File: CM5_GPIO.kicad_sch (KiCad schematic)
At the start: 29 parts, among them J14 JST_SHBM04B-SRSS-TB, J16 JST_SHBM04B-SRSS-TB, J2 Conn_02x07_Odd_Even, J3 Conn_01x03, J7 Micro_SD_Card_Det, J8 THD-20-R, J9 THD-02-R, SW1 Right angle Tact button, SW2 Right angle Tact button, U1 TPD4EUSB30, U18 RT9742GGJ5, U2 TPD4EUSB30, U3 MagJack-A70-112-331N126, U5 74LVC1G07SE-7, U9 SK6812

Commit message: starting to trace
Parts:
- added J19: Conn_01x03, Connector_PinHeader_2.54mm:PinHeader_1x03_P2.54mm_Vertical, symbol Connector_Generic:Conn_01x03
- SW2: footprint Button_Switch_THT:SW_Tactile_SPST_Angled_PTS645Vx58-2LFS -> Button_Switch_THT:SW_Tactile_SPST_Angled_PTS645Vx31-2LFS
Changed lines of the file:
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@@
 			)
 		)
-		(property "Footprint" "Button_Switch_THT:SW_Tactile_SPST_Angled_PTS645Vx58-2LFS"
+		(property "Footprint" "Button_Switch_THT:SW_Tactile_SPST_Angled_PTS645Vx31-2LFS"
 			(at 86.36 158.75 0)
 			(effects
@@
 					(unit 1)
 				)
+			)
+		)
+	)
+	(symbol
+		(lib_id "Connector_Generic:Conn_01x03")
+		(at 143.51 113.03 0)
+		(unit 1)
+		(exclude_from_sim no)
+		(in_bom yes)
+		(on_board yes)
+		(dnp no)
+		(fields_autoplaced yes)
+		(property "Reference" "J19"
+			(at 146.05 111.7599 0)
+			(effects
+				(font
+					(size 1.27 1.27)
+				)
+				(justify left)
+			)
+		)
+		(property "Value" "Conn_01x03"
+			(at 146.05 114.2999 0)
+			(effects
+				(font
+					(size 1.27 1.27)
+				)
+				(justify left)
+			)
+		)
+		(property "Footprint" "Connector_PinHeader_2.54mm:PinHeader_1x03_P2.54mm_Vertical"
+			(at 143.51 113.03 0)
+			(effects
+				(font
+					(size 1.27 1.27)
+				)
+				(hide yes)
+			)
+		)
+		(property "Datasheet" "~"
+			(at 143.51 113.03 0)
+			(effects
+				(font
+					(size 1.27 1.27)
+				)
+				(hide yes)
+			)
+		)
+		(property "Description" "Generic connector, single row, 01x03, script generated (kicad-library-utils/schlib/autogen/connector/)"
+			(at 143.51 113.03 0)
+			(effects
+				(font
+					(size 1.27 1.27)
+				)
+				(hide yes)
+			)
+		)
+		(pin "2"
+		)
+		(pin "3"
+		)
+		(pin "1"
+		)
+		(instances
+			(project ""
+				(path "/e63e39d7-6ac0-4ffd-8aa3-1841a4541b55/00000000-0000-0000-0000-00005cff706a"
+					(reference "J19")
+					(unit 1)
+				)

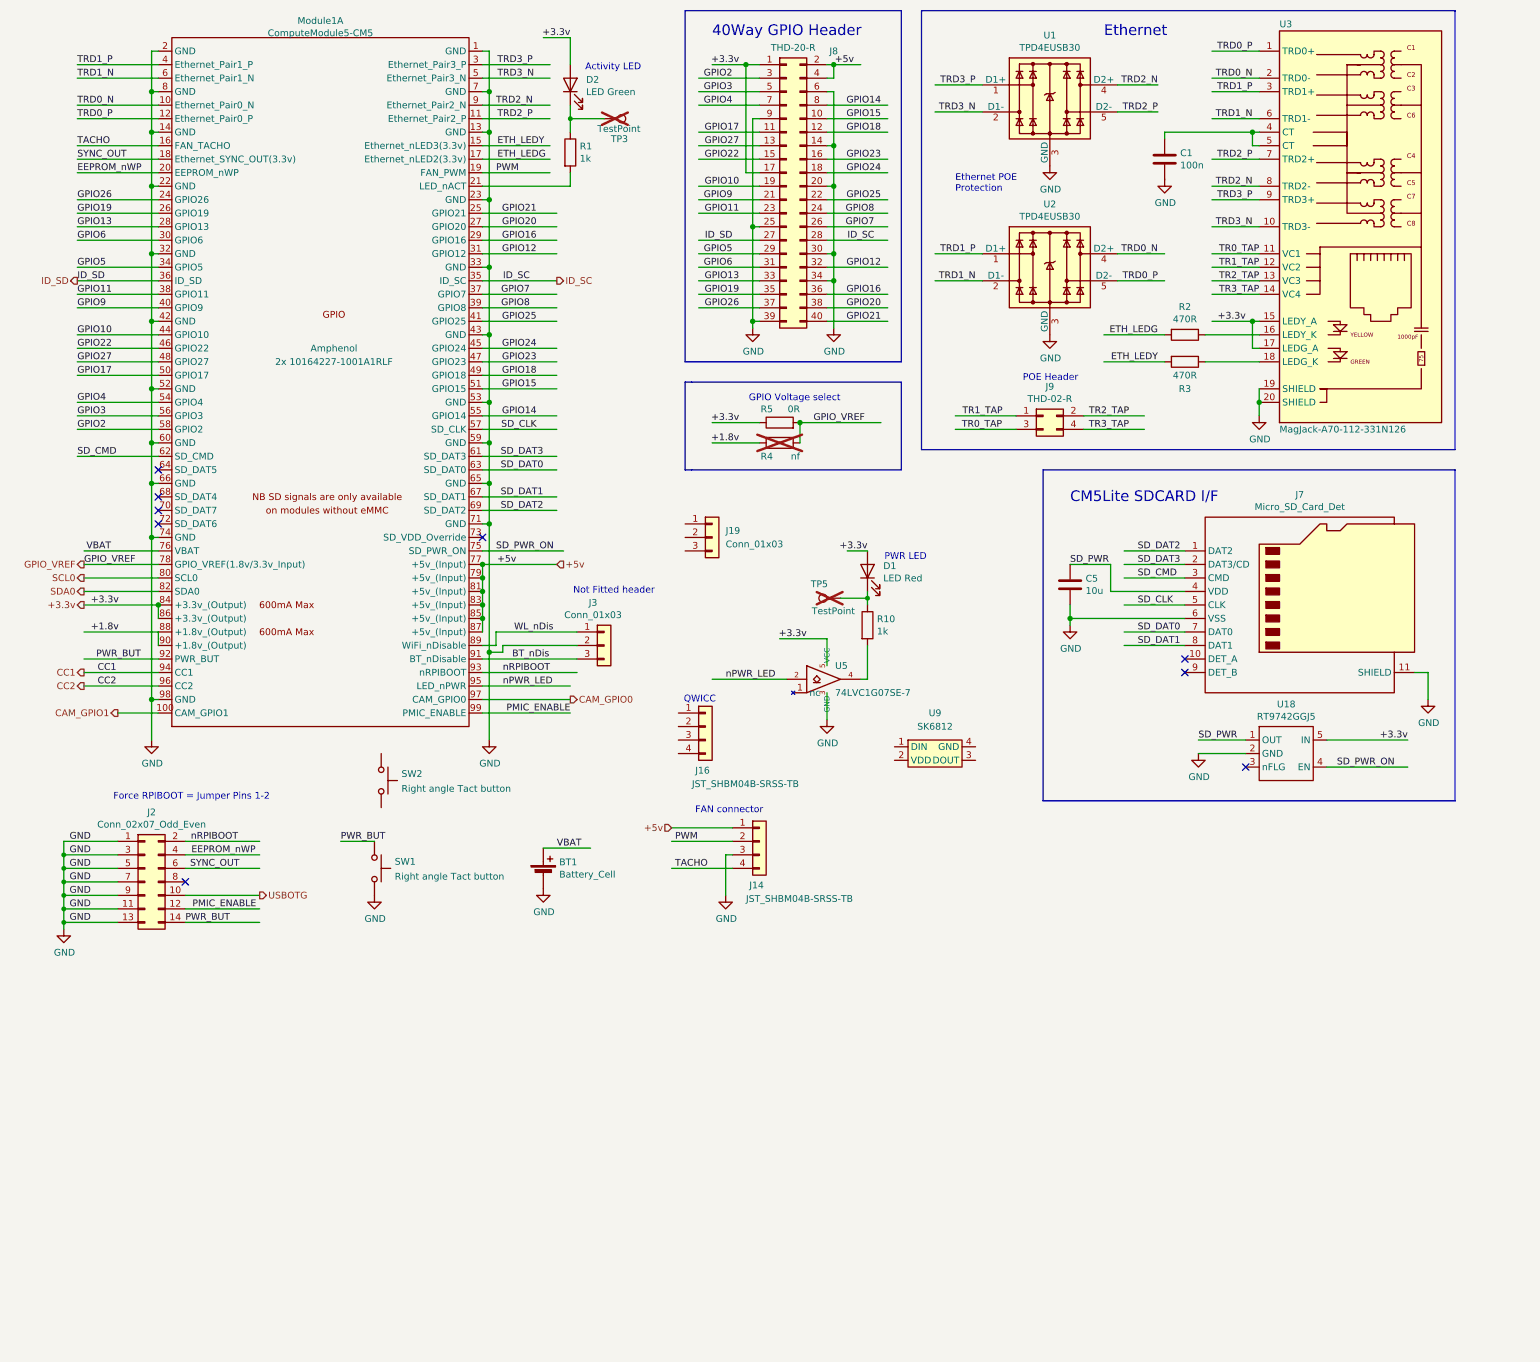
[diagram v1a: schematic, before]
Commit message: voltage regulator refactoring
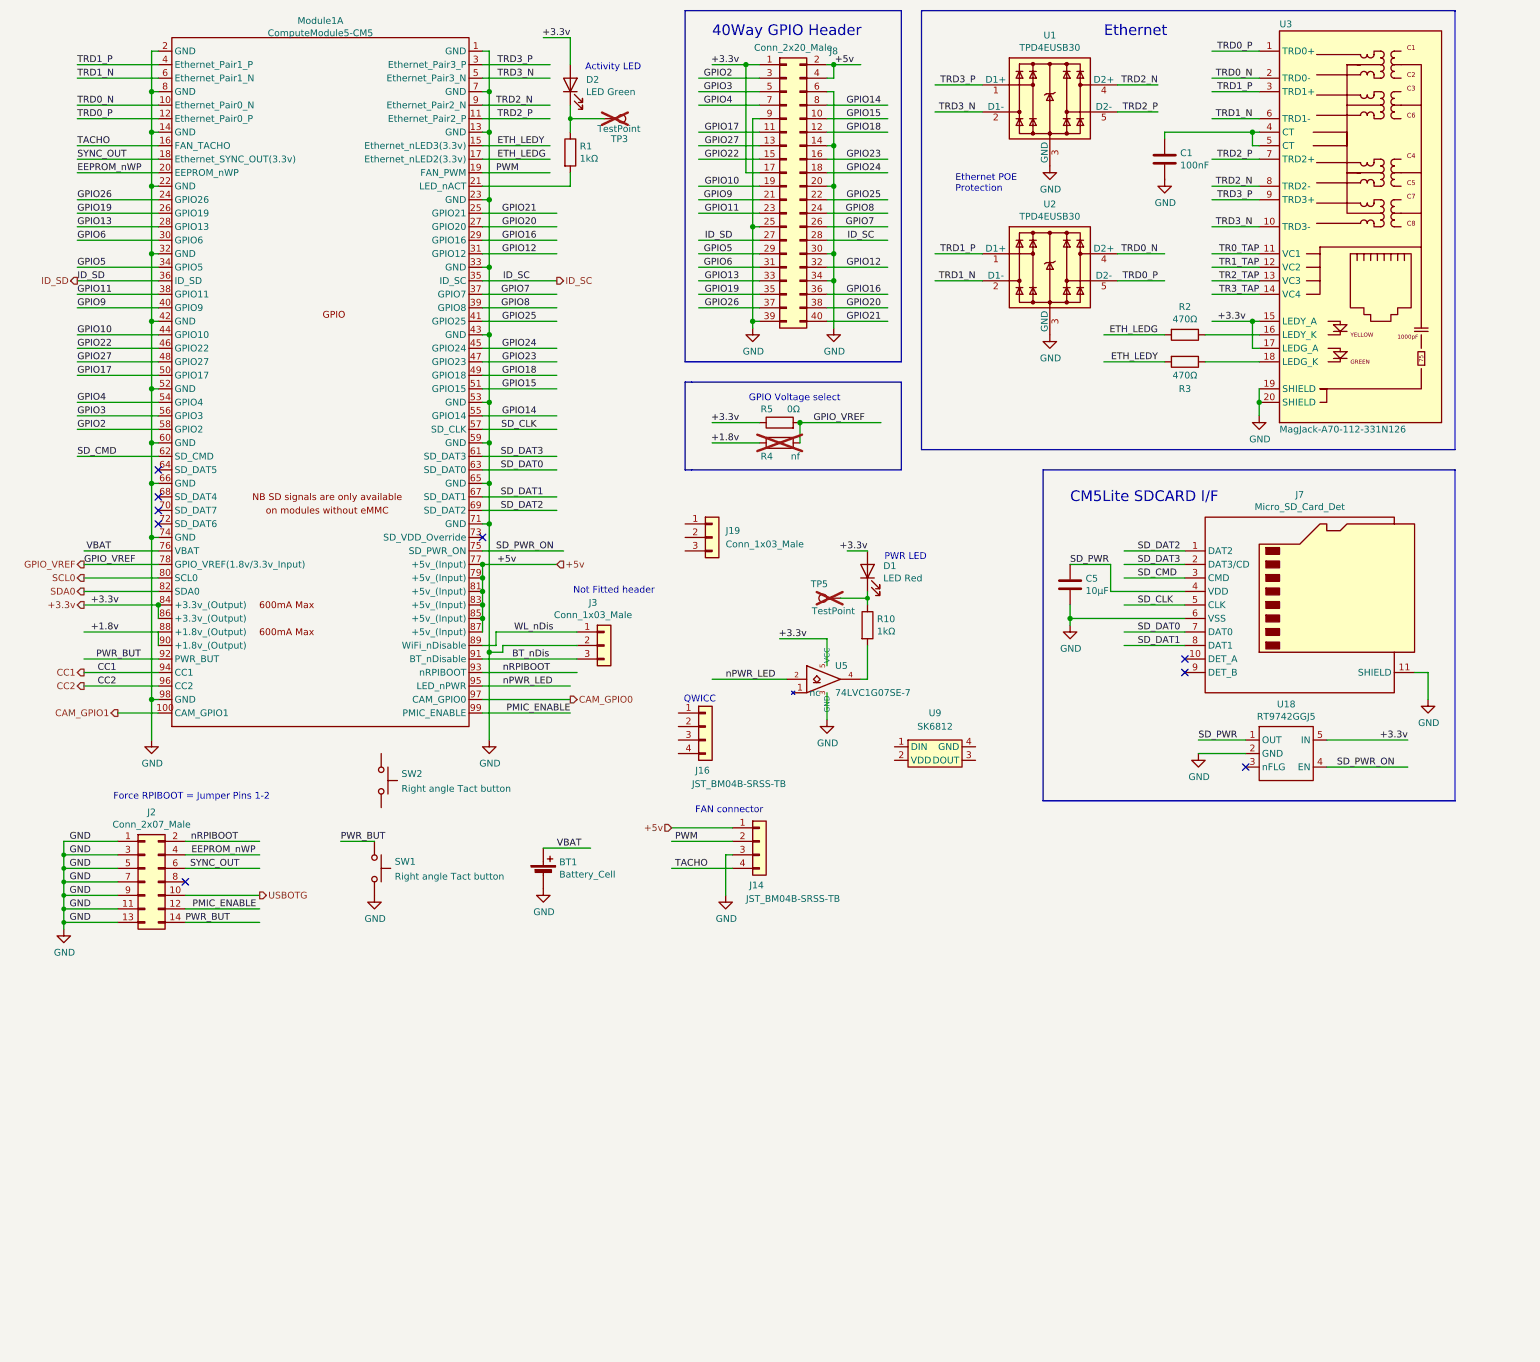
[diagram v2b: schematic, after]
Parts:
- removed J9: THD-02-R, Connector_PinHeader_2.54mm:PinHeader_2x02_P2.54mm_Vertical, symbol Connector_Generic:Conn_02x02_Odd_Even
- BT1: Dist. P/N (none) -> 36-3034-ND; Distributor (none) -> Digikey; Field4 Digikey -> (none); Field5 36-3034-ND -> (none); Field6 3034 -> (none); Field7 Keystone -> (none); Manf. P/N (none) -> 3034; Manufacturer (none) -> Keystone; Part Description Battery Retainer Coin, 20.0mm 1 Cell SMD (SMT) Tab -> Retainer, Battery, 20.0mm 1 Cell SMD (SMT) Tab
- C1: value 100n -> 100nF; Dist. P/N (none) -> 478-11504-2-ND; Distributor (none) -> Digikey; Field4 Farnell -> (none); Field5 2611911 -> (none); Field6 RM EMK105 B7104KV-F -> (none); Field7 TAIYO YUDEN EUROPE GMBH -> (none); Field8 110091611 -> (none); Manf. P/N (none) -> 04026D104KAT4A; Manufacturer (none) -> Kyocera; Part Description 0.1uF 10% 16V Ceramic Capacitor X7R 0402 (1005 Metric) -> Capacitor, Ceramic, 0.1µF, ±10%, 6.3V, X5R, 0402 (1005m)
- C5: value 10u -> 10µF; Dist. P/N (none) -> 478-KGM21AR51A106KUTR-ND; Distributor (none) -> Digikey; Field4 Digikey -> (none); Field5 490-14381-1-ND -> (none); Field6 GRM21BR71A106KA73L -> (none); Field7 Murata -> (none); Field8 111893011 -> (none); Manf. P/N (none) -> 0805ZD106KAT2A; Manufacturer (none) -> Kyocera; Part Description 10uF 10% 10V Ceramic Capacitor X7R 0805 (2012 Metric) -> Capacitor, Ceramic, 10µF, ±10%, 10V, X5R, 0805 (2012m)
- D1: Dist. P/N (none) -> 160-1479-2-ND; Distributor (none) -> Digikey; Field4 Digikey -> (none); Field5 LTST-S270KRKT -> (none); Field6 SML-A12U8TT86Q -> (none); Field7 Rohm -> (none); Manf. P/N (none) -> LTST-S270KRKT; Manufacturer (none) -> Lite-On Inc.; Part Description Red 620nm LED Indication - Discrete 2.2V 2-SMD, No Lead -> LED, Red, 620nm, 2.2V, SMD 0603
- D2: Dist. P/N (none) -> 160-1478-2-ND; Distributor (none) -> Digikey; Field4 Digikey -> (none); Field5 LTST-S270KGKT -> (none); Field6 SML-A12M8TT86N -> (none); Field7 Rohm -> (none); Manf. P/N (none) -> LTST-S270KGKT; Manufacturer (none) -> Lite-On Inc.; Part Description Green 572nm LED Indication - Discrete 2.2V 2-SMD, No Lead -> LED, Green, 572nm, 2.2V, SMD 0603
- J14, J16: value JST_SHBM04B-SRSS-TB -> JST_BM04B-SRSS-TB; Dist. P/N (none) -> 455-BM04B-SRSS-TBTR-ND; Distributor (none) -> Digikey; Field5 SHBM04B-SRSS-TB -> (none); Field6 SHBM04B-SRSS-TB -> (none); Field7 JST -> (none); Manf. P/N (none) -> BM04B-SRSS-TB; Manufacturer (none) -> JST; Part Description 4 pin vertical 1mm pitch connector -> Connector, Male, 1x04, vertical, 1mm P
- J19: value Conn_01x03 -> Conn_1x03_Male; Dist. P/N (none) -> 900-0022032031-ND; Distributor (none) -> Digikey; Manf. P/N (none) -> 0022032031; Manufacturer (none) -> Molex; Part Description (none) -> Pin Header, Male, 1x03, 2.54mm P, Vertical
- J2: value Conn_02x07_Odd_Even -> Conn_2x07_Male; Dist. P/N (none) -> WM9875-ND; Distributor (none) -> Digikey; Field4 Toby -> (none); Field5 THD-07-R -> (none); Field6 THD-07-R -> (none); Field7 Toby -> (none); Manf. P/N (none) -> 0010897140; Manufacturer (none) -> Molex; Part Description PinHeader_2x07_P2.54mm_Vertical -> Pin Header, Male, 2x07, 2.54mm P, Vertical
- J3: value Conn_01x03 -> Conn_1x03_Male; Dist. P/N (none) -> 900-0022032031-ND; Distributor (none) -> Digikey; Field4 nf -> (none); Field5 nf -> (none); Field6 nf -> (none); Field7 nf -> (none); Manf. P/N (none) -> 0022032031; Manufacturer (none) -> Molex; Part Description 3pin 0.1" connector -> Pin Header, Male, 1x03, 2.54mm P, Vertical
- J7: Dist. P/N (none) -> 2358234; Distributor (none) -> Farnell; Field4 Farnell -> (none); Field5 2358234 -> (none); Field6 503398-1892 -> (none); Field7 Molex -> (none); Manf. P/N (none) -> 503398-1892; Manufacturer (none) -> Molex
- J8: value THD-20-R -> Conn_2x20_Male; Dist. P/N (none) -> WM19411-ND; Distributor (none) -> Digikey; Field4 Toby -> (none); Field5 THD-20-R -> (none); Field6 THD-20-R -> (none); Field7 Toby -> (none); Field8 UCON00511 -> (none); Manf. P/N (none) -> 0010897400; Manufacturer (none) -> Molex; Part Description PinHeader_2x20_P2.54mm_Vertical -> Pin Header, Male, 2x20, 2.54mm P, Vertical
- Module1: Dist. P/N (none) -> 609-10164227-1001A1RLFTR-ND; Distributor (none) -> Digikey; Field4 Amphenol -> (none); Field5 2x 10164227-1001A1RLF -> (none); Field6 2x 10164227-1001A1RLF -> (none); Field7 Hirose -> (none); Manf. P/N (none) -> 10164227-1001A1RLF x2; Manufacturer (none) -> Amphenol; Part Description 100 Position Connector Receptacle, Center Strip Contacts Su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 -> Connector, CM Receptacle, 100 pin, 0.4mm P
- R1, R10: value 1k -> 1kΩ; Dist. P/N (none) -> 10-ERJ-H2RF1001XTR-ND; Distributor (none) -> Digikey; Field4 Farnell -> (none); Field5 9239235 -> (none); Field6 RK73H1ETTP1001F -> (none); Field7 KOA EUROPE GMBH -> (none); Field8 125049511 -> (none); Manf. P/N (none) -> ERJ-H2RF1001X; Manufacturer (none) -> Panasonic; Part Description Resistor 1K M1005 1% 63mW -> Resistor, 1kΩ, ±1%, 0.1W, SMD 0402 (1005m)
- R2, R3: value 470R -> 470Ω; Dist. P/N (none) -> P470LTR-ND; Distributor (none) -> Digikey; Field4 Farnell -> (none); Field5 9239197 -> (none); Field6 RK73G1ETQTP4700D -> (none); Field7 KOA EUROPE GMBH -> (none); Field8 120887981 -> (none); Manf. P/N (none) -> ERJ-2RKF4700X; Manufacturer (none) -> Panasonic; Part Description Resistor 470R M1005 1% 63mW -> Resistor, 470Ω, ±1%, 0.1W, SMD 0402 (1005m)
- R4: Dist. P/N (none) -> nf; Distributor (none) -> nf; Field4 nf -> (none); Field5 nf -> (none); Field6 nf -> (none)
- R5: value 0R -> 0Ω; Dist. P/N (none) -> P0.0ATR-ND; Distributor (none) -> Digikey; Field4 Farnell -> (none); Field5 9233750 -> (none); Field6 MCR10EZPJ000 -> (none); Field7 Rohm -> (none); Field8 121629591 -> (none); Manf. P/N (none) -> ERJ-6GEY0R00V; Manufacturer (none) -> Panasonic; Part Description Resistor 0R M2012 5% -> Resistor, Jumper, 0Ω, SMD 0805 (2012m)
- SW1, SW2: Dist. P/N (none) -> CKN9120-ND; Distributor (none) -> Digikey; Field5 PTS645VH58-2LFS -> (none); Field6 PTS645VH58-2LFS -> (none); Field7 CK -> (none); Manf. P/N (none) -> PTS645VH58-2 LFS; Manufacturer (none) -> C&K; Part Description Right angle through hole Tact switch -> Switch, Tactile, SPST-NO, Right Angle
- TP3, TP5: Dist. P/N (none) -> nf; Distributor (none) -> nf; Field4 nf -> (none); Field5 nf -> (none); Field6 nf -> (none); Field7 nf -> (none)
- U1, U2: Dist. P/N (none) -> 296-28063-2-ND; Distributor (none) -> Digikey; Field4 Farnell -> (none); Field5 2335455 -> (none); Field6 CDDFN10-3324P-13 -> (none); Field7 Bourns -> (none); Field8 UDIO00346 -> (none); Manf. P/N (none) -> TPD4EUSB30DQAR; Manufacturer (none) -> Texas Instruments; Part Description Quad TVS diode for high speed signals (USB3, GigE etc.) -> Diode, TVS, 8V clamp, 1A
- U18: Dist. P/N (none) -> 1028-1436-2-ND; Distributor (none) -> Digikey; Field4 Farnell -> (none); Field5 2545875 -> (none); Field6 RT9742GGJ5 -> (none); Field7 RichTek -> (none); Field8 USWI00166 -> (none); Manf. P/N (none) -> RT9742GGJ5; Manufacturer (none) -> RichTek; Part Description Power Switch/Driver 1:1 N-Channel 1A TSOT-23-5 -> Power Switch/Driver, 1:1, N-Channel, 1A, TSOT-23-5
- U3: Dist. P/N (none) -> 931-TMJG4926HENL-ND; Distributor (none) -> Digikey; Field5 TRJG0926HENL -> (none); Field6 TRJG0926HENL -> (none); Field7 Trxcon -> (none); Field8 UCON00900 -> (none); Manf. P/N (none) -> TMJG4926HENL; Manufacturer (none) -> Taoglas Limited; Part Description Gigabit Ethernet Magjack -> Receptacle, RJ45, 1Gb
- U5: Dist. P/N (none) -> 74LVC1G07SE-7DITR-ND; Distributor (none) -> Digikey; Field4 Farnell -> (none); Field5 2425492 -> (none); Field6 74LVC1G07SE-7 -> (none); Field7 Diodes -> (none); Manf. P/N (none) -> 74LVC1G07SE-7; Manufacturer (none) -> Diodes Inc.; Part Description Buffer, Non-Inverting 1 Element 1 Bit per Element Open Drai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 -> Buffer, Non-Inverting, 1 Element, 1 Bit per Element, Open D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
- U9: Dist. P/N (none) -> C2890037; Distributor (none) -> LSCS; Manf. P/N (none) -> SK6812SIDE-A-RVS; Manufacturer (none) -> OPSCO; Part Description (none) -> LED, RGB, 475-620nm, 3.7v-5.5v, SMD
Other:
- note removed: "POE Header"

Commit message: place all components
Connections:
- net +5v: now also U9.2 (VDD)
- net GND: now also U9.4 (GND)
- no-connect marks 9 -> 11

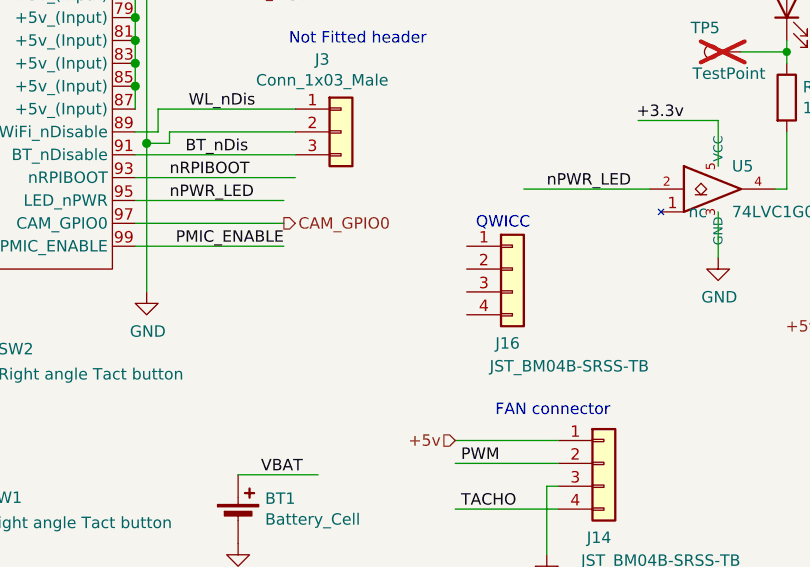
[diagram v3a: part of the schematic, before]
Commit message: change C27-C29 to 1206, reroute i2c
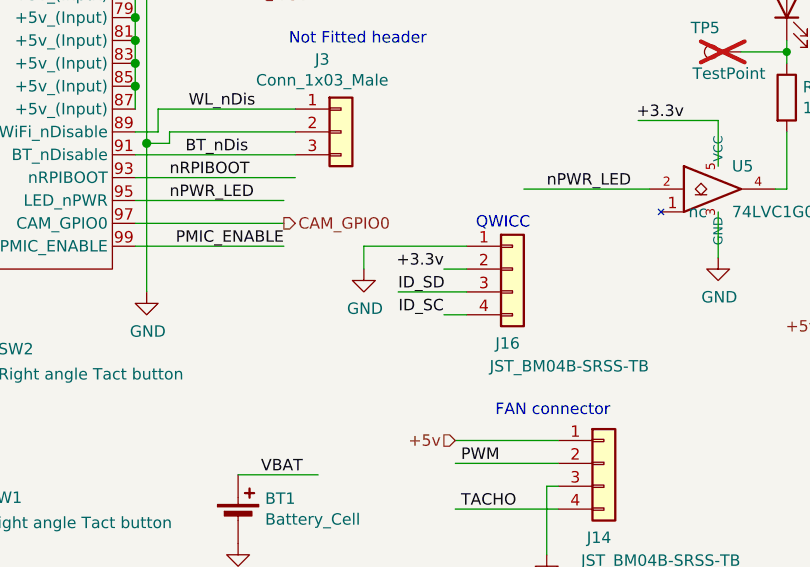
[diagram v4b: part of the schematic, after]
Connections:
- net +3.3v: now also J16.2 (Pin_2)
- net GND: now also J16.1 (Pin_1)
- net ID_SC: now also J16.4 (Pin_4)
- net ID_SD: now also J16.3 (Pin_3)
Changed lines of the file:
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@@
 	(wire
 		(pts
+			(xy 125.73 148.59) (xy 125.73 146.05)
+		)
+		(stroke
+			(width 0)
+			(type default)
+		)
+	)
+	(wire
+		(pts
 			(xy 166.37 46.99) (xy 165.1 46.99)
 		)
@@
 	(wire
 		(pts
+			(xy 125.73 146.05) (xy 137.16 146.05)
+		)
+		(stroke
+			(width 0)
+			(type default)
+		)
+	)
+	(wire
+		(pts
 			(xy 101.6 49.53) (xy 101.6 62.23)
 		)
@@
 	(wire
 		(pts
+			(xy 134.62 153.67) (xy 137.16 153.67)
+		)
+		(stroke
+			(width 0)
+			(type default)
+		)
+	)
+	(wire
+		(pts
 			(xy 100.33 74.93) (xy 101.6 74.93)
 		)
@@
 	(wire
 		(pts
+			(xy 134.62 148.59) (xy 137.16 148.59)
+		)
+		(stroke
+			(width 0)
+			(type default)
+		)
+	)
+	(wire
+		(pts
 			(xy 100.33 52.07) (xy 114.3 52.07)
 		)
@@
 	(wire
 		(pts
+			(xy 129.54 151.13) (xy 137.16 151.13)
+		)
+		(stroke
+			(width 0)
+			(type default)
+		)
+	)
+	(wire
+		(pts
 			(xy 39.37 143.51) (xy 38.1 143.51)
 		)
@@
 		)
 	)
+	(label "ID_SC"
+		(at 134.62 153.67 180)
+		(effects
+			(font
+				(size 1.27 1.27)
+			)
+			(justify right bottom)
+		)
+	)
 	(label "TR2_TAP"
 		(at 246.38 64.77 180)
@@
 		)
 	)
+	(label "ID_SD"
+		(at 129.54 151.13 0)
+		(effects
+			(font
+				(size 1.27 1.27)
+			)
+			(justify left bottom)
+		)
+	)
 	(label "+1.8v"
 		(at 26.67 130.81 0)
@@
 		)
 	)
+	(label "+3.3v"
+		(at 134.62 148.59 180)
+		(effects
+			(font
+				(size 1.27 1.27)
+			)
+			(justify right bottom)
+		)
+	)
 	(label "PWR_BUT"
 		(at 27.686 135.89 0)
@@
 					(unit 1)
 				)
+			)
+		)
+	)
+	(symbol
+		(lib_id "power:GND")
+		(at 125.73 148.59 0)
+		(unit 1)
+		(exclude_from_sim no)
+		(in_bom yes)
+		(on_board yes)
+		(dnp no)
+		(property "Reference" "#PWR039"
+			(at 125.73 154.94 0)
+			(effects
+				(font
+					(size 1.27 1.27)
+				)
+				(hide yes)
+			)
+		)
+		(property "Value" "GND"
+			(at 125.857 152.9842 0)
+			(effects
+				(font
+					(size 1.27 1.27)
+				)
+			)
+		)
+		(property "Footprint" ""
+			(at 125.73 148.59 0)
+			(effects
+				(font
+					(size 1.27 1.27)
+				)
+				(hide yes)
+			)
+		)
+		(property "Datasheet" ""
+			(at 125.73 148.59 0)
+			(effects
+				(font
+					(size 1.27 1.27)
+				)
+				(hide yes)
+			)
+		)
+		(property "Description" "Power symbol creates a global label with name \"GND\" , ground"
+			(at 125.73 148.59 0)
+			(effects
+				(font
+					(size 1.27 1.27)
+				)
+				(hide yes)
+			)
+		)
+		(pin "1"
+		)
+		(instances
+			(project "libreboard"
+				(path "/e63e39d7-6ac0-4ffd-8aa3-1841a4541b55/00000000-0000-0000-0000-00005cff706a"
+					(reference "#PWR039")
+					(unit 1)
+				)

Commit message: cleanup, testpoints
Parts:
- removed BT1: Battery_Cell, CM5IO:BatteryHolder_Keystone_3034_1x20mm, symbol Device:Battery_Cell
- added TP10: TestPoint I2C SDA1, TestPoint:TestPoint_Pad_D1.5mm, symbol Connector:TestPoint
- added TP11: TestPoint I2C SCL1, TestPoint:TestPoint_Pad_D1.5mm, symbol Connector:TestPoint
- added TP12, TP16: TestPoint I2C +3.3V, TestPoint:TestPoint_Pad_D1.5mm, symbol Connector:TestPoint
- added TP13, TP17: TestPoint I2C GND, TestPoint:TestPoint_Pad_D1.5mm, symbol Connector:TestPoint
- added TP14: TestPoint I2C SDA0, TestPoint:TestPoint_Pad_D1.5mm, symbol Connector:TestPoint
- added TP15: TestPoint I2C SCL0, TestPoint:TestPoint_Pad_D1.5mm, symbol Connector:TestPoint
- added TP8: TestPoint +3.3V, TestPoint:TestPoint_Pad_D1.5mm, symbol Connector:TestPoint
- added TP9: TestPoint GND, TestPoint:TestPoint_Pad_D1.5mm, symbol Connector:TestPoint
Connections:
- net +3.3v: now also TP12.1, TP16.1, TP8.1
- net GND: now also J19.1 (Pin_1), SW2.2, TP13.1, TP17.1, TP9.1
- net GPIO14: now also J19.2 (Pin_2)
- net GPIO15: now also J19.3 (Pin_3)
- net ID_SC: now also TP11.1
- net ID_SD: now also TP10.1
- net SCL0: now also TP15.1
- net SDA0: now also TP14.1
- net nRPIBOOT: now also SW2.1
- net VBAT: no longer names the net of Module1.76 (VBAT)
- no-connect marks 11 -> 12
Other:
- moved on the sheet: SW1, SW2
